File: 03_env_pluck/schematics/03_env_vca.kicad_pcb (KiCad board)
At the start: 2 copper layers, 50 x 150 mm, 38 parts, among them J1 Gate In 1, J2 Gate In 2, J3 Eurorack 10 pin, J4 Env Out 1, J5 Env Out 2, SW1 Pluck / AD, SW2 Pluck / AD, U1 TL074

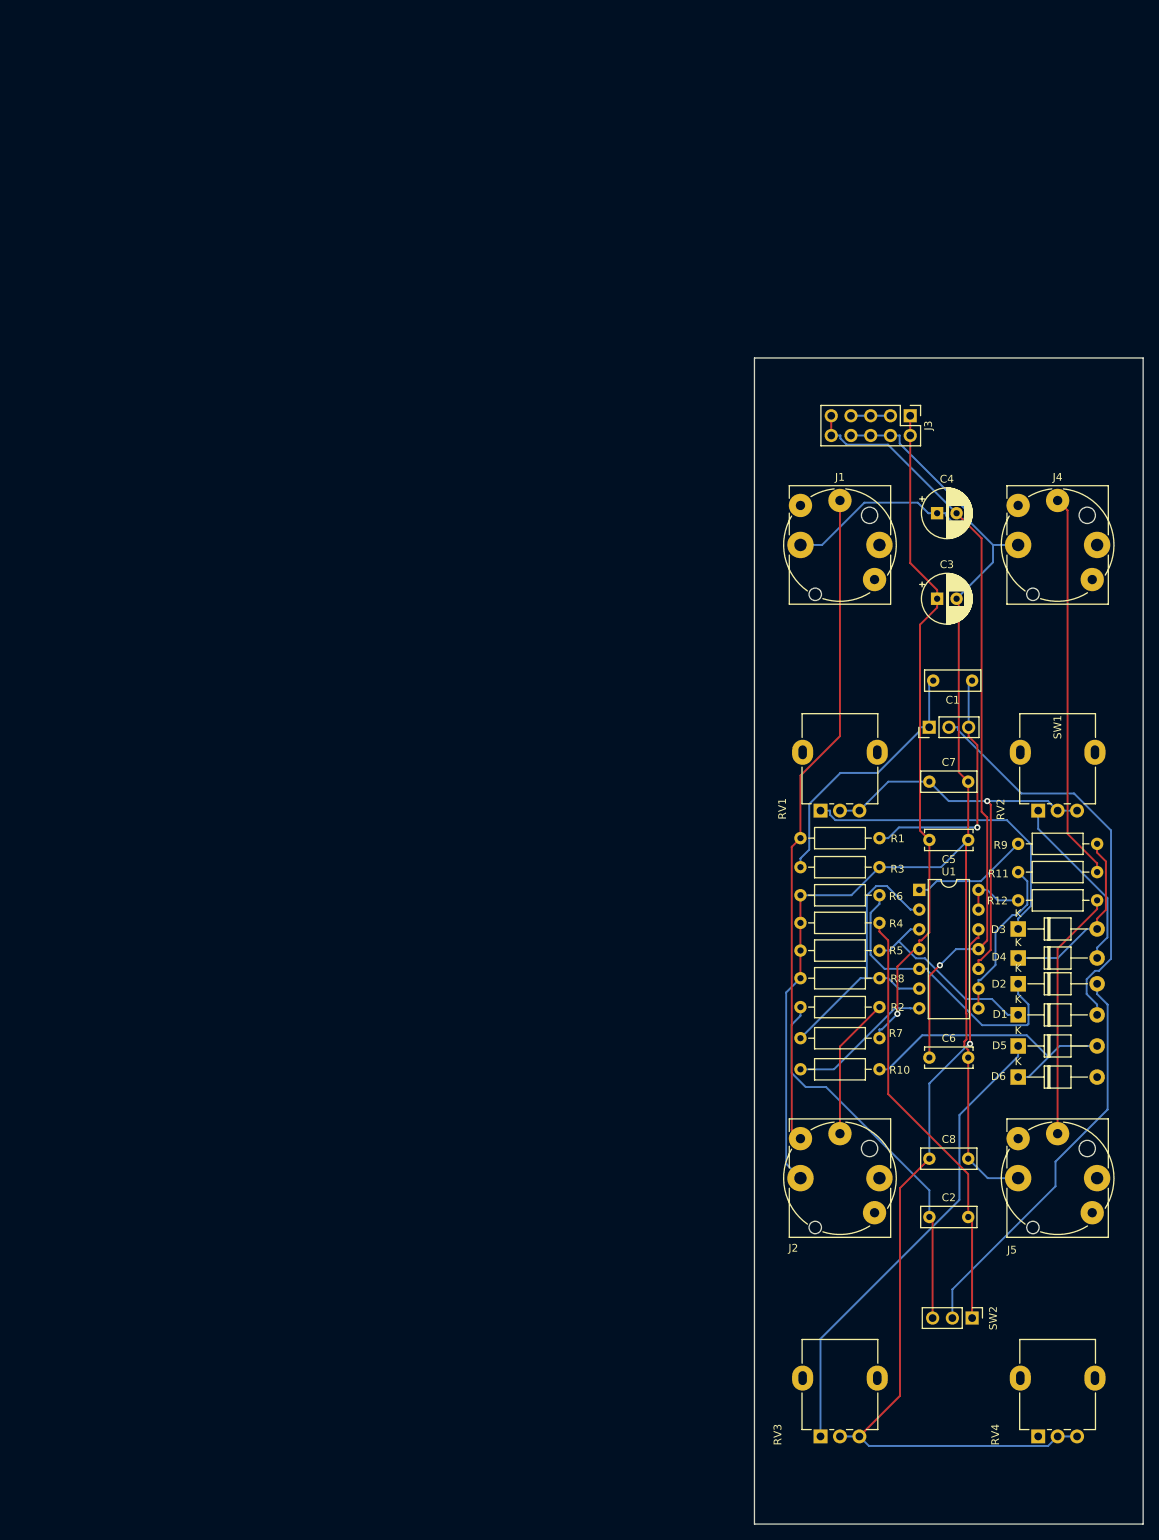
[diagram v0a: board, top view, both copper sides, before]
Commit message: added PCB for 03
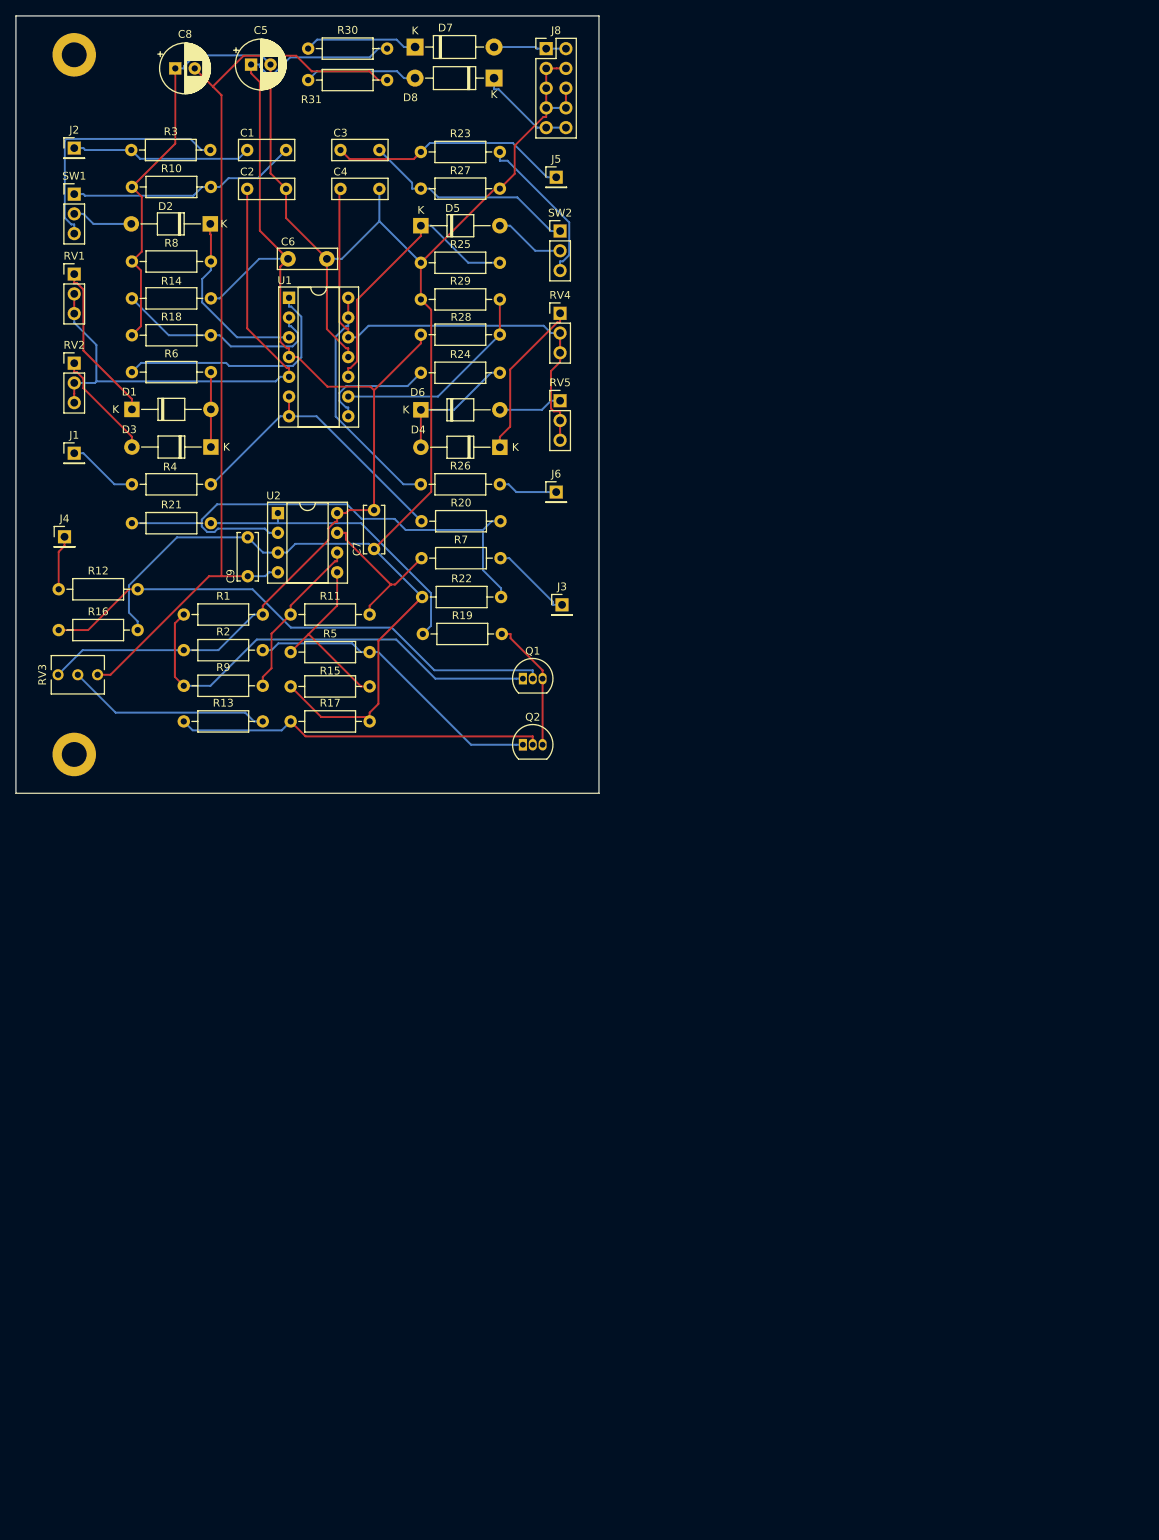
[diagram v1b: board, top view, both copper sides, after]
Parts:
- added C9: 100nF, Capacitor_THT:C_Disc_D6.0mm_W2.5mm_P5.00mm, F.Cu at (29.8, 72.1)
- added D7: 1N5819, Diode_THT:D_DO-41_SOD81_P10.16mm_Horizontal, F.Cu at (51.3, 4.00)
- added D8: 1N5819, Diode_THT:D_DO-41_SOD81_P10.16mm_Horizontal, F.Cu at (61.5, 8.00)
- added J6: env out 2, Connector_PinHeader_2.54mm:PinHeader_1x01_P2.54mm_Vertical, F.Cu at (69.5, 61.2)
- added J8: Eurorack, Connector_PinHeader_2.54mm:PinHeader_2x05_P2.54mm_Vertical, F.Cu at (68.2, 4.21)
- added MH1: MountingHole_3.2mm_M3_DIN965_Pad, MountingHole:MountingHole_3.2mm_M3_DIN965_Pad, F.Cu at (7.50, 5.00)
- added MH2: MountingHole_3.2mm_M3_DIN965_Pad, MountingHole:MountingHole_3.2mm_M3_DIN965_Pad, F.Cu at (7.50, 95.0)
- added Q1: BC547, Package_TO_SOT_THT:TO-92_Inline, F.Cu at (65.2, 85.2)
- added Q2: BC547, Package_TO_SOT_THT:TO-92_Inline, F.Cu at (65.2, 93.8)
- added R13: 100k, Resistor_THT:R_Axial_DIN0207_L6.3mm_D2.5mm_P10.16mm_Horizontal, F.Cu at (21.6, 90.8)
- added R14: 82k, Resistor_THT:R_Axial_DIN0207_L6.3mm_D2.5mm_P10.16mm_Horizontal, F.Cu at (14.9, 36.3)
- added R15: 100k, Resistor_THT:R_Axial_DIN0207_L6.3mm_D2.5mm_P10.16mm_Horizontal, F.Cu at (35.3, 86.2)
- added R16: 100R, Resistor_THT:R_Axial_DIN0207_L6.3mm_D2.5mm_P10.16mm_Horizontal, F.Cu at (5.50, 79.0)
- added R17: 100R, Resistor_THT:R_Axial_DIN0207_L6.3mm_D2.5mm_P10.16mm_Horizontal, F.Cu at (35.3, 90.8)
- added R18: 18k, Resistor_THT:R_Axial_DIN0207_L6.3mm_D2.5mm_P10.16mm_Horizontal, F.Cu at (14.9, 41.1)
- added R19: 10k, Resistor_THT:R_Axial_DIN0207_L6.3mm_D2.5mm_P10.16mm_Horizontal, F.Cu at (52.3, 79.5)
- added R20: 100k, Resistor_THT:R_Axial_DIN0207_L6.3mm_D2.5mm_P10.16mm_Horizontal, F.Cu at (52.2, 65.0)
- added R21: 82k, Resistor_THT:R_Axial_DIN0207_L6.3mm_D2.5mm_P10.16mm_Horizontal, F.Cu at (14.9, 65.2)
- added R22: 100k, Resistor_THT:R_Axial_DIN0207_L6.3mm_D2.5mm_P10.16mm_Horizontal, F.Cu at (52.2, 74.8)
- added R23: 100k, Resistor_THT:R_Axial_DIN0207_L6.3mm_D2.5mm_P10.16mm_Horizontal, F.Cu at (52.1, 17.5)
- added R24: 560R, Resistor_THT:R_Axial_DIN0207_L6.3mm_D2.5mm_P10.16mm_Horizontal, F.Cu at (52.1, 45.9)
- added R25: 100k, Resistor_THT:R_Axial_DIN0207_L6.3mm_D2.5mm_P10.16mm_Horizontal, F.Cu at (52.1, 31.8)
- added R26: 1k, Resistor_THT:R_Axial_DIN0207_L6.3mm_D2.5mm_P10.16mm_Horizontal, F.Cu at (52.1, 60.2)
- added R27: 100k, Resistor_THT:R_Axial_DIN0207_L6.3mm_D2.5mm_P10.16mm_Horizontal, F.Cu at (62.2, 22.2)
- added R28: 82k, Resistor_THT:R_Axial_DIN0207_L6.3mm_D2.5mm_P10.16mm_Horizontal, F.Cu at (62.2, 41.0)
- added R29: 18k, Resistor_THT:R_Axial_DIN0207_L6.3mm_D2.5mm_P10.16mm_Horizontal, F.Cu at (52.1, 36.5)
- added R30: 10, Resistor_THT:R_Axial_DIN0207_L6.3mm_D2.5mm_P10.16mm_Horizontal, F.Cu at (37.6, 4.20)
- added R31: 10, Resistor_THT:R_Axial_DIN0207_L6.3mm_D2.5mm_P10.16mm_Horizontal, F.Cu at (37.6, 8.25)
- added RV5: 1M, Connector_PinHeader_2.54mm:PinHeader_1x03_P2.54mm_Vertical, F.Cu at (70.0, 49.5)
- added U2: TL072, Package_DIP:DIP-8_W7.62mm_Socket, F.Cu at (33.7, 64.0)
- C2: value 47nF -> 1uF
- C3: value 47uF -> 47nF; footprint Capacitor_THT:CP_Radial_D6.3mm_P2.50mm -> Capacitor_THT:C_Rect_L7.0mm_W2.5mm_P5.00mm
- C4: value 47uF -> 1uF; footprint Capacitor_THT:CP_Radial_D6.3mm_P2.50mm -> Capacitor_THT:C_Rect_L7.0mm_W2.5mm_P5.00mm
- C5: value 100nF -> 50uF; footprint Capacitor_THT:C_Disc_D6.0mm_W2.5mm_P5.00mm -> Capacitor_THT:CP_Radial_D6.3mm_P2.50mm
- C6: footprint Capacitor_THT:C_Disc_D6.0mm_W2.5mm_P5.00mm -> Capacitor_THT:C_Disc_D7.5mm_W2.5mm_P5.00mm
- C7: value 1uF -> 100nF; footprint Capacitor_THT:C_Rect_L7.0mm_W2.5mm_P5.00mm -> Capacitor_THT:C_Disc_D6.0mm_W2.5mm_P5.00mm
- C8: value 1uF -> 50uF; footprint Capacitor_THT:C_Rect_L7.0mm_W2.5mm_P5.00mm -> Capacitor_THT:CP_Radial_D6.3mm_P2.50mm
- J1: value Gate In 1 -> env out 1; footprint Connector_Audio:Jack_6.35mm_Neutrik_NJ5FD-V_Vertical -> Connector_PinHeader_2.54mm:PinHeader_1x01_P2.54mm_Vertical
- J2: value Gate In 2 -> gate In 1; footprint Connector_Audio:Jack_6.35mm_Neutrik_NJ5FD-V_Vertical -> Connector_PinHeader_2.54mm:PinHeader_1x01_P2.54mm_Vertical
- J3: value Eurorack 10 pin -> signal out; footprint Connector_PinHeader_2.54mm:PinHeader_2x05_P2.54mm_Vertical -> Connector_PinHeader_2.54mm:PinHeader_1x01_P2.54mm_Vertical
- J4: value Env Out 1 -> signal in; footprint Connector_Audio:Jack_6.35mm_Neutrik_NJ5FD-V_Vertical -> Connector_PinHeader_2.54mm:PinHeader_1x01_P2.54mm_Vertical
- J5: value Env Out 2 -> gate In 2; footprint Connector_Audio:Jack_6.35mm_Neutrik_NJ5FD-V_Vertical -> Connector_PinHeader_2.54mm:PinHeader_1x01_P2.54mm_Vertical
- R1, R2: value 100k -> 20k
- R10: value 560R -> 100k
- R11, R12: value 1k -> 100k
- R4: value 100k -> 1k
- R5: value 100k -> 10k
- R6: value 100k -> 560R
- R7: value 82k -> 1k
- R8: value 18k -> 100k
- R9: value 560R -> 10k
- RV1, RV2, RV4: footprint Potentiometer_THT:Potentiometer_Alpha_RD901F-40-00D_Single_Vertical -> Connector_PinHeader_2.54mm:PinHeader_1x03_P2.54mm_Vertical
- RV3: value 1M -> 100k; footprint Potentiometer_THT:Potentiometer_Alpha_RD901F-40-00D_Single_Vertical -> Potentiometer_THT:Potentiometer_Vishay_T73XW_Horizontal
- SW1: value Pluck / AD -> Pluck / AD 1
- SW2: value Pluck / AD -> Pluck / AD 2
- U1: value TL074 -> LM324; footprint Package_DIP:DIP-14_W7.62mm -> Package_DIP:DIP-14_W7.62mm_Socket
- moved C8 170.5 mm to (20.5, 6.75)
- moved J2 160.5 mm to (7.50, 17.0)
- moved C2 158.7 mm to (29.8, 22.2)
- moved RV4 157.0 mm to (70.0, 38.2), turned to 0 degrees
- moved SW2 149.5 mm to (70.0, 27.7), turned to 0 degrees
- moved D2 142.7 mm to (25.0, 26.8), turned to 180 degrees
- moved R10 142.4 mm to (14.9, 22.0)
- moved J5 138.9 mm to (69.5, 20.8)
- moved RV3 138.6 mm to (5.42, 84.8)
- moved D1 138.1 mm to (14.9, 50.6)
- moved RV2 136.7 mm to (7.50, 44.7), turned to 0 degrees
- moved C5 135.9 mm to (30.2, 6.25), turned to 0 degrees
- moved R3 133.3 mm to (14.8, 17.2), turned to 0 degrees
- moved C6 131.8 mm to (35.0, 31.2)
- moved D5 130.5 mm to (52.1, 27.0)
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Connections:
- C1 pad 1: Net-(SW1-C) -> Net-(J2-Pin_1)
- C2 pad 1: Net-(SW2-C) -> Net-(U1B-+)
- C2 pad 2: Net-(SW2-A) -> GNDREF
- C3 pad 1: +12V -> Net-(J5-Pin_1)
- C3 pad 2: GNDREF -> Net-(SW2-A)
- C4 pad 1: GNDREF -> Net-(U1D-+)
- C4 pad 2: -12V -> GNDREF
- C5 pad 1: GNDREF -> +12V
- C5 pad 2: +12V -> GNDREF
- C6 pad 1: -12V -> +12V
- C7 pad 1: Net-(U1C-+) -> GNDREF
- C7 pad 2: GNDREF -> +12V
- C8 pad 1: Net-(U1D-+) -> GNDREF
- C8 pad 2: GNDREF -> -12V
- D3 pad 1: Net-(D3-K) -> Net-(D1-A)
- D4 pad 1: Net-(D3-A) -> Net-(D4-K)
- D6 pad 1: Net-(D5-A) -> Net-(D4-A)
- J3 pad 1: +12V -> Net-(J3-Pin_1)
- R1 pad 1: Net-(J1-PadT) -> Net-(Q1-C)
- R1 pad 2: Net-(SW1-C) -> +12V
- R10 pad 1: Net-(R10-Pad1) -> GNDREF
- R10 pad 2: Net-(D5-A) -> Net-(SW1-A)
- R11 pad 1: Net-(U1C--) -> Net-(U2B--)
- R11 pad 2: Net-(J4-PadT) -> Net-(R11-Pad2)
- R12 pad 1: Net-(U1D--) -> Net-(J4-Pin_1)
- R12 pad 2: Net-(J5-PadT) -> Net-(Q1-B)
- R2 pad 1: Net-(J2-PadT) -> +12V
- R2 pad 2: Net-(SW2-C) -> Net-(Q2-C)
- R3 pad 1: GNDREF -> Net-(J2-Pin_1)
- R3 pad 2: Net-(SW1-A) -> Net-(SW1-C)
- R4 pad 1: GNDREF -> Net-(U1B--)
- R4 pad 2: Net-(SW2-A) -> Net-(J1-Pin_1)
- R5 pad 1: GNDREF -> Net-(U2B-+)
- R5 pad 2: Net-(D1-K) -> Net-(Q2-C)
- R6 pad 1: GNDREF -> Net-(R6-Pad1)
- R6 pad 2: Net-(D2-K) -> Net-(D1-A)
- R7 pad 1: Net-(U1A--) -> Net-(R11-Pad2)
- R7 pad 2: +12V -> Net-(J3-Pin_1)
- R8 pad 2: Net-(U1A--) -> Net-(D2-K)
- R9 pad 1: Net-(R9-Pad1) -> Net-(Q1-C)
- R9 pad 2: Net-(D3-A) -> Net-(U2B--)
- RV1 pad 1: Net-(D3-K) -> Net-(D1-K)
- RV1 pad 2: Net-(U1C-+) -> Net-(U1B-+)
- RV1 pad 3: Net-(U1C-+) -> Net-(U1B-+)
- RV2 pad 1: Net-(D4-A) -> Net-(D3-A)
- RV2 pad 2: Net-(U1C-+) -> Net-(U1B-+)
- RV2 pad 3: Net-(U1C-+) -> Net-(U1B-+)
- RV3 pad 1: Net-(D5-K) -> +12V
- RV3 pad 2: Net-(U1D-+) -> Net-(R13-Pad2)
- RV3 pad 3: Net-(U1D-+) -> -12V
- RV4 pad 1: Net-(D6-A) -> Net-(D4-K)
- SW1 pad 2: Net-(D1-A) -> Net-(D2-A)
- SW2 pad 2: Net-(D2-A) -> Net-(D5-A)
- U1 pad 1: Net-(R9-Pad1) -> Net-(R6-Pad1)
- U1 pad 10: Net-(U1C-+) -> Net-(D5-K)
- U1 pad 11: -12V -> GNDREF
- U1 pad 3: Net-(D1-K) -> Net-(D2-K)
- U1 pad 5: Net-(D2-K) -> Net-(U1B-+)
- U1 pad 6: Net-(U1A--) -> Net-(U1B--)
- U1 pad 7: Net-(R10-Pad1) -> Net-(U1B--)
- U1 pad 8: Net-(U1C--) -> Net-(R24-Pad1)
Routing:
- net Net-(J1-PadT): track 85.1 -> 0.00 mm
- net +12V: track 86.5 -> 161.5 mm, vias 1 -> 0
- net Net-(U2A--): track 0.00 -> 71.0 mm
- net GNDREF: track 205.3 -> 276.1 mm
- net Net-(U1B-+): track 0.00 -> 69.5 mm
- net Net-(Q1-B): track 0.00 -> 68.5 mm
- net Net-(Q1-C): track 0.00 -> 58.3 mm
- net Net-(U1C-+): track 56.2 -> 0.00 mm, vias 1 -> 0
- net Net-(J4-PadT): track 49.9 -> 0.00 mm
- net Net-(Q2-B): track 0.00 -> 47.7 mm
- net Net-(D2-A): track 51.8 -> 7.87 mm
- net Net-(D1-A): track 52.4 -> 9.64 mm
- net Net-(D3-K): track 40.8 -> 0.00 mm
- net Net-(U1D-+): track 103.3 -> 63.3 mm, vias 1 -> 0
- net Net-(Q2-C): track 0.00 -> 39.2 mm
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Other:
- board size 50 x 150 mm -> 75 x 100 mm

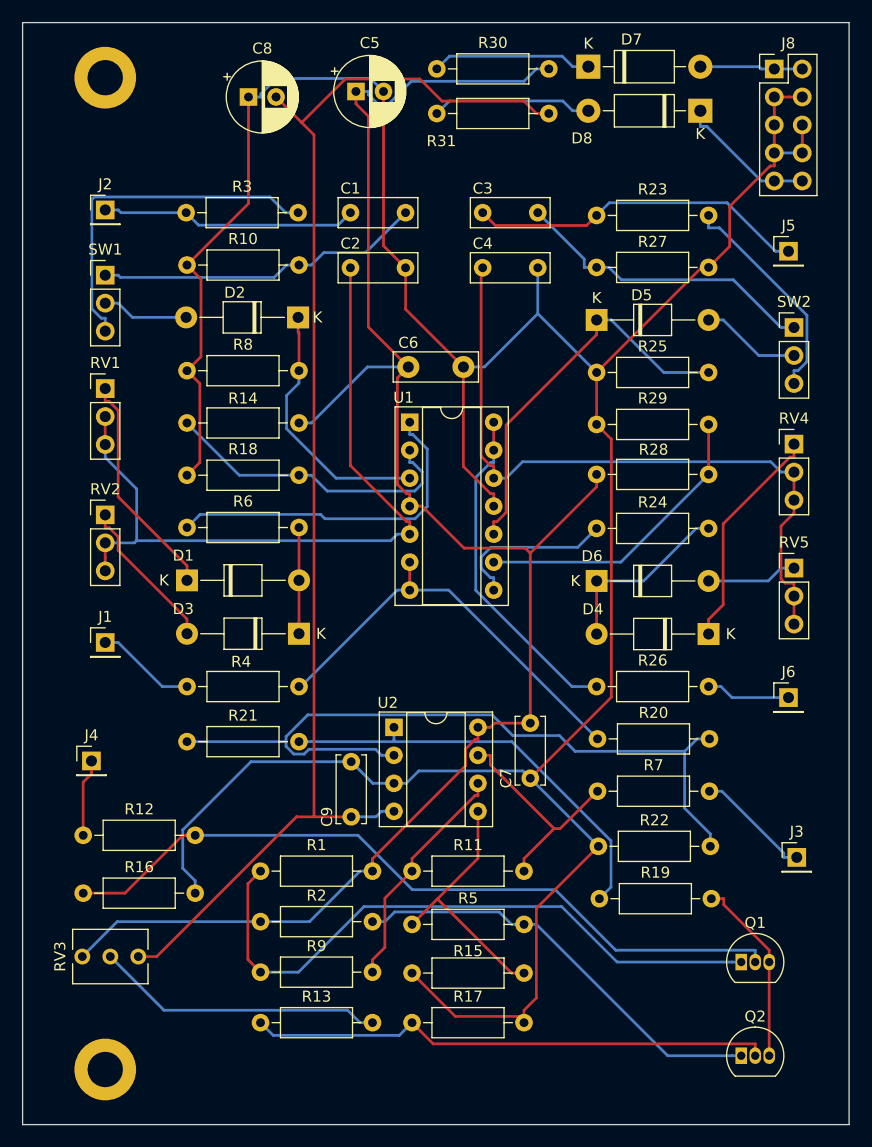
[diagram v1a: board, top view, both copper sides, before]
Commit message: updated PCBs for 02 and 03
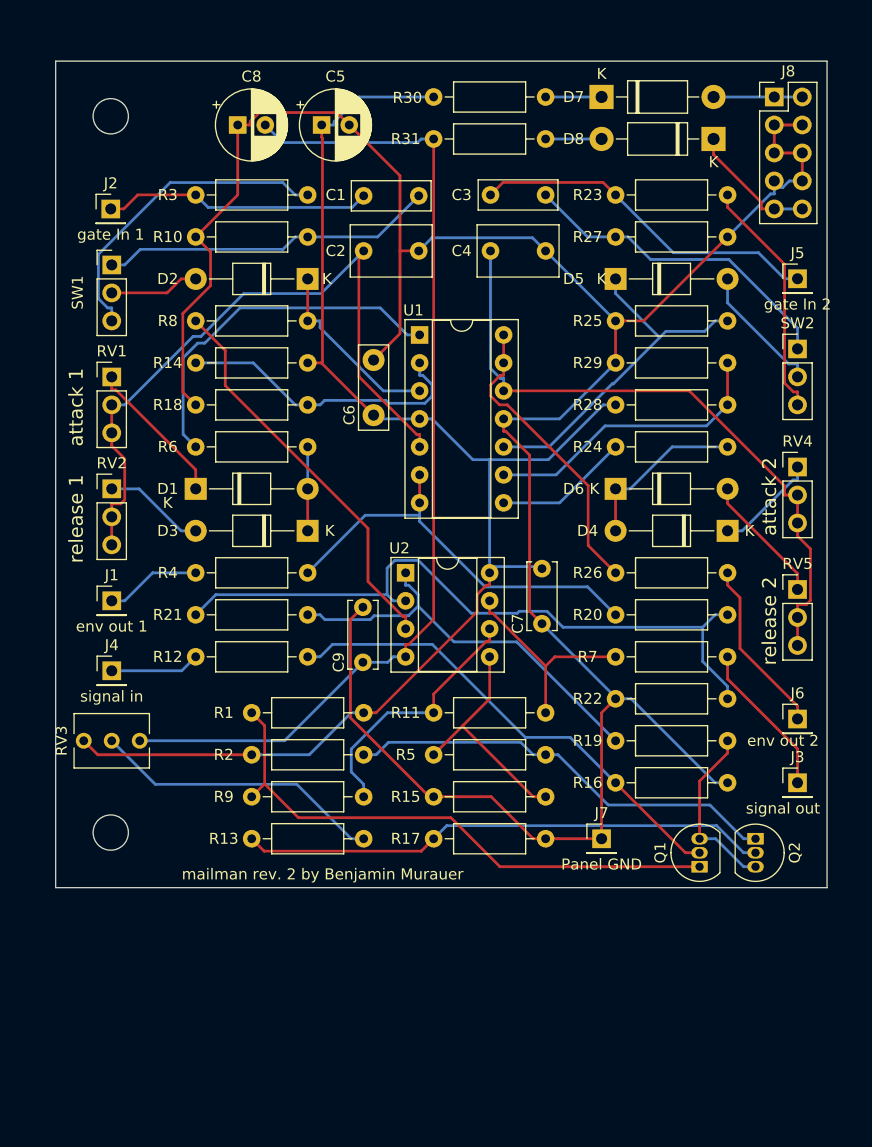
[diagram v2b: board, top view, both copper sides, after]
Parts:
- removed MH1, MH2: MountingHole_3.2mm_M3_DIN965_Pad, MountingHole:MountingHole_3.2mm_M3_DIN965_Pad
- added H1: MountingHole, MountingHole:MountingHole_3.2mm_M3, F.Cu at (8.00, 8.50)
- added H2: MountingHole, MountingHole:MountingHole_3.2mm_M3, F.Cu at (8.00, 73.5)
- added J7: Panel GND, Connector_PinHeader_2.54mm:PinHeader_1x01_P2.54mm_Vertical, F.Cu at (52.5, 74.1)
- C2, C4: footprint Capacitor_THT:C_Rect_L7.0mm_W2.5mm_P5.00mm -> Capacitor_THT:C_Rect_L7.2mm_W4.5mm_P5.00mm_FKS2_FKP2_MKS2_MKP2
- moved R16 49.3 mm to (53.8, 69.0)
- moved Q2 19.7 mm to (66.5, 74.1), turned to -90 degrees
- moved RV3 19.6 mm to (5.55, 65.2)
- moved R12 19.1 mm to (15.7, 57.5)
- moved R17 16.8 mm to (37.3, 74.1)
- moved R13 16.7 mm to (20.8, 74.1)
- moved R15 16.1 mm to (37.3, 70.2)
- moved R9 15.9 mm to (20.8, 70.2)
- moved R5 15.5 mm to (37.3, 66.4)
- moved R2 15.2 mm to (20.8, 66.4)
- moved R11 14.5 mm to (37.3, 62.6)
- moved R19 14.4 mm to (53.8, 65.2)
- moved R1 14.4 mm to (20.8, 62.6)
- moved U2 14.1 mm to (34.8, 49.9)
- moved C7 14.1 mm to (47.1, 54.5)
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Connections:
- C2 pad 2: GNDREF -> GND
- C4 pad 2: GNDREF -> GND
- C5 pad 2: GNDREF -> GND
- C6 pad 2: GNDREF -> GND
- C7 pad 1: GNDREF -> GND
- C8 pad 1: GNDREF -> GND
- C9 pad 2: GNDREF -> GND
- J8 pad 3: GNDREF -> GND
- J8 pad 4: GNDREF -> GND
- J8 pad 5: GNDREF -> GND
- J8 pad 6: GNDREF -> GND
- J8 pad 7: GNDREF -> GND
- J8 pad 8: GNDREF -> GND
- R10 pad 1: GNDREF -> GND
- R15 pad 1: GNDREF -> GND
- R16 pad 2: GNDREF -> GND
- R17 pad 2: GNDREF -> GND
- R18 pad 1: GNDREF -> GND
- R22 pad 1: GNDREF -> GND
- R25 pad 1: GNDREF -> GND
- R27 pad 1: GNDREF -> GND
- R29 pad 1: GNDREF -> GND
- U1 pad 11: GNDREF -> GND
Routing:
- net GNDREF: track 276.1 -> 36.0 mm
- net GND: track 0.00 -> 231.2 mm
- net +12V: track 161.5 -> 127.5 mm
- net -12V: track 120.8 -> 91.6 mm
- net Net-(Q1-B): track 68.5 -> 43.9 mm
- net Net-(D4-K): track 20.7 -> 9.44 mm
- net Net-(D7-K): track 14.6 -> 5.08 mm
- net Net-(D8-A): track 14.6 -> 5.08 mm
- net Net-(J6-Pin_1): track 7.66 -> 15.9 mm
- net Net-(D1-K): track 20.7 -> 13.5 mm
- net Net-(Q1-C): track 58.3 -> 51.2 mm
- net Net-(U2A--): track 71.0 -> 64.2 mm
- net Net-(D2-K): track 23.6 -> 17.0 mm
- net Net-(U1B-+): track 69.5 -> 63.2 mm
- net Net-(D3-A): track 14.1 -> 9.20 mm
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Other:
- board size 75 x 100 mm -> 70 x 75 mm
- board text added: "mailman rev. 2 by Benjamin Murauer"
